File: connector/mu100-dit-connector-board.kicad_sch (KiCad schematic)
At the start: 8 parts, among them J1 Conn_01x17_Male, J2 51247 Molex, J3 JST-PH_01x10_Socket

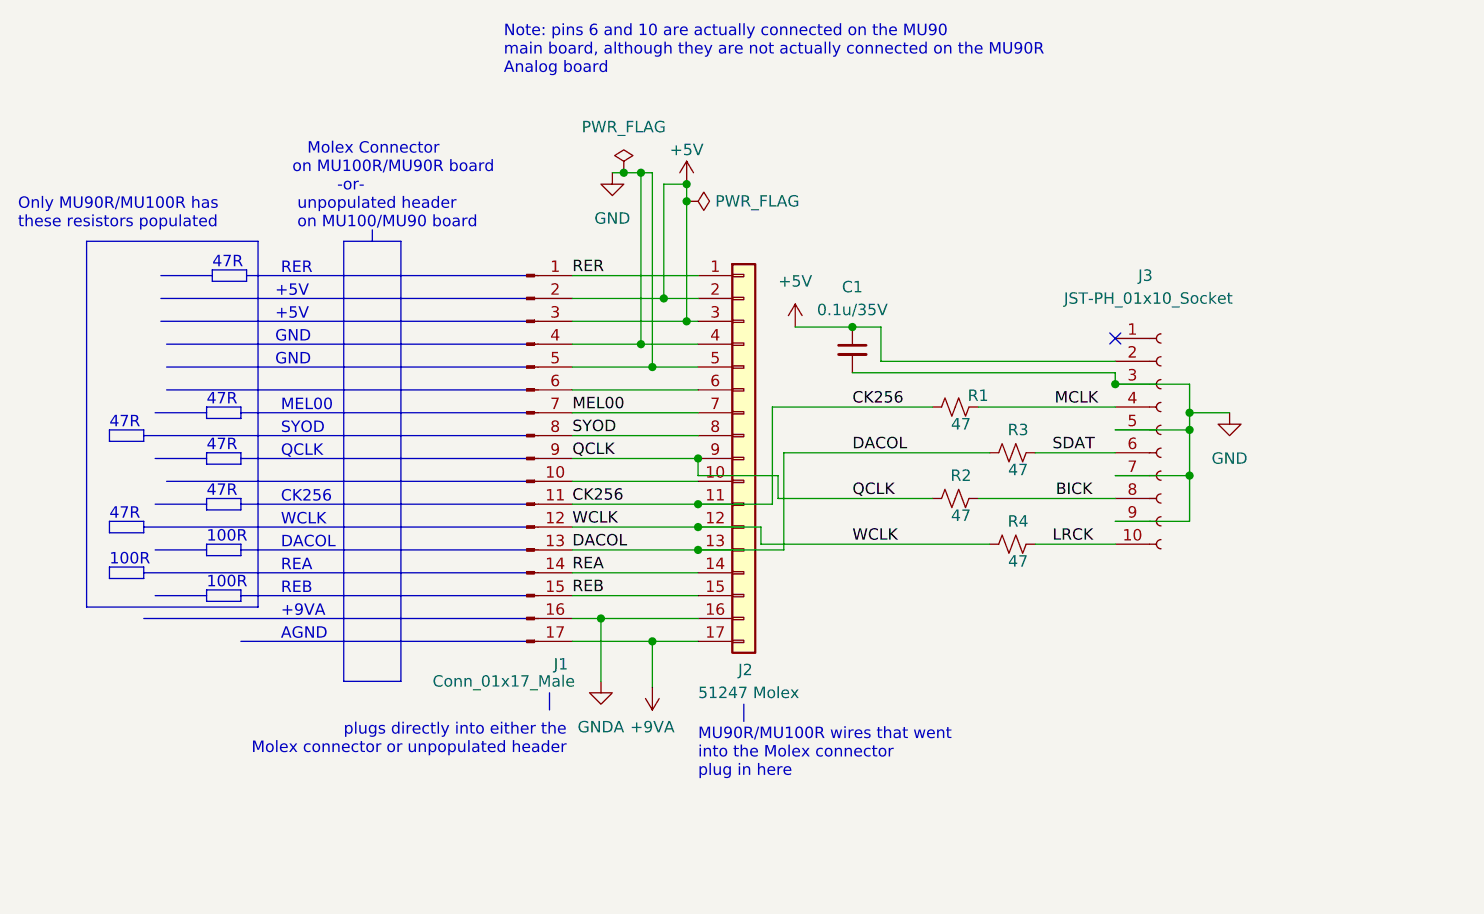
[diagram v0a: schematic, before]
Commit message: Clean up schematics and board drawings
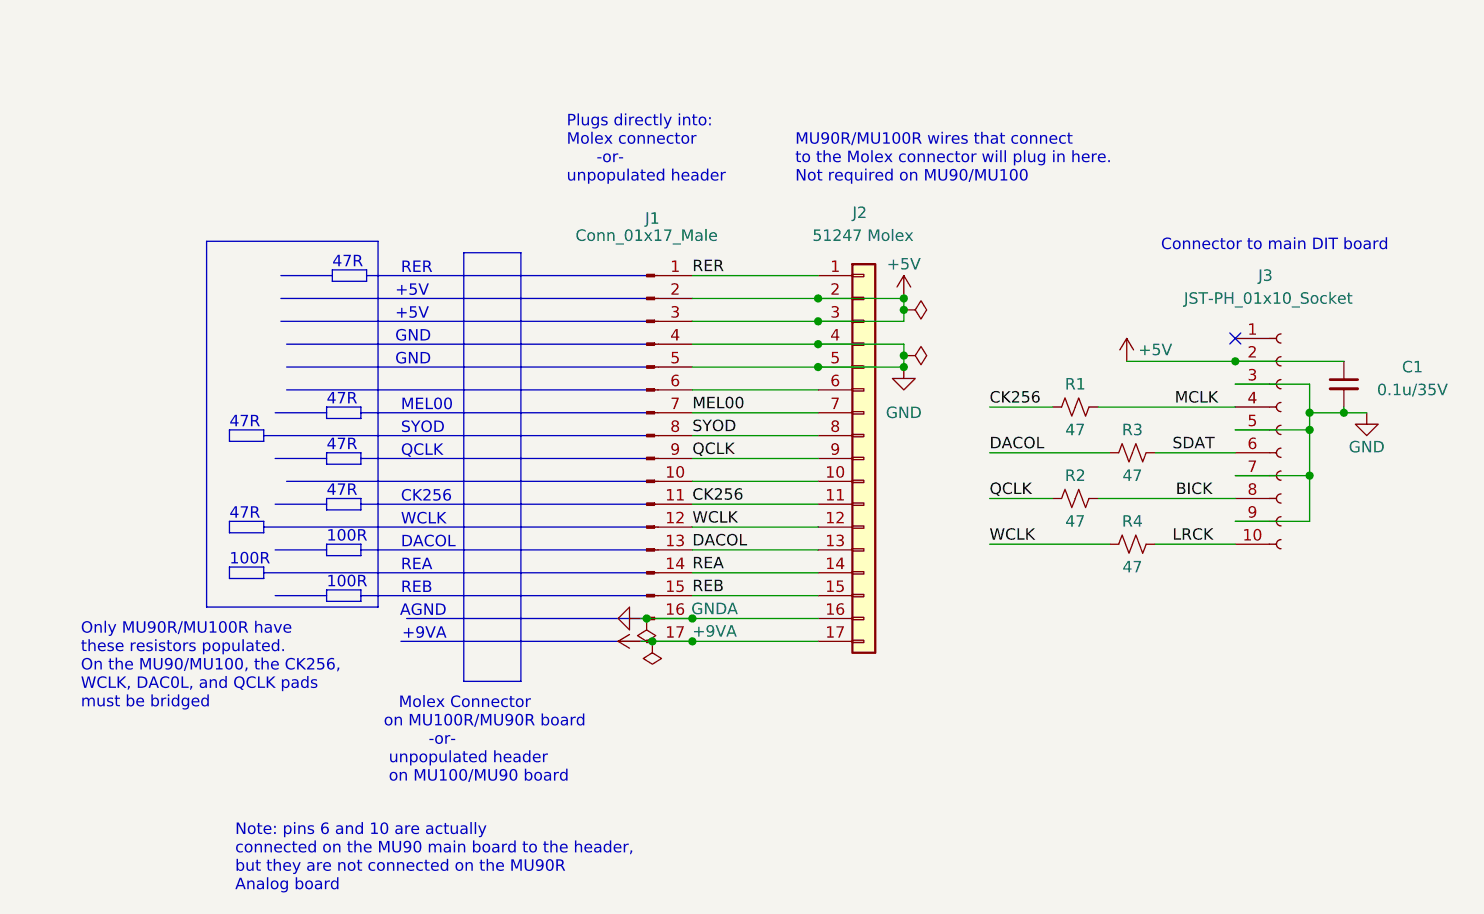
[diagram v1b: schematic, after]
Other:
- note added: "Connector to main DIT board"
- note added: "MU90R/MU100R wires that connect to the Molex connector will plug in here. Not required on MU90/MU100"
- note added: "Note: pins 6 and 10 are actually connected on the MU90 main board to the header, but they are not connected on the MU90R Analog board"
- note added: "Only MU90R/MU100R have these resistors populated. On the MU90/MU100, the CK256, WCLK, DAC0L, and QCLK pads must be bridged"
- note added: "Plugs directly into: Molex connector -or- unpopulated header"
- note removed: "MU90R/MU100R wires that went into the Molex connector plug in here"
- note removed: "Note: pins 6 and 10 are actually connected on the MU90 main board, although they are not actually connected on the MU90R Analog board"
- note removed: "Only MU90R/MU100R has these resistors populated"
- note removed: "plugs directly into either the Molex connector or unpopulated header"
- moved on the sheet: C1, J1, J2, J3, R1, R2, R3, R4

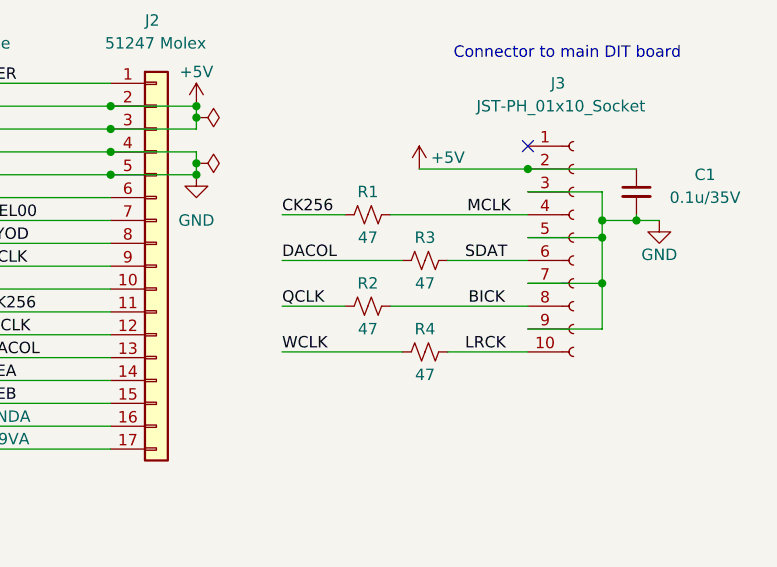
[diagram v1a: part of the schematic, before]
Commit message: remove terminating resistors on connector board
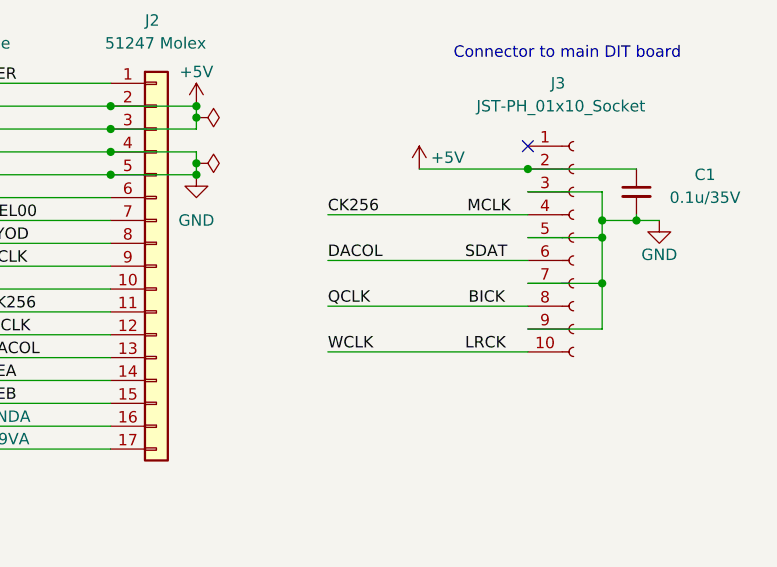
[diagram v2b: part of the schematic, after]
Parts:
- removed R1, R2, R3, R4: 47, Resistor_SMD:R_0805_2012Metric_Pad1.20x1.40mm_HandSolder, symbol Device:R_Small_US
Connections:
- net MCLK is gone; now on net CK256: J3.4 (Pin_4)
- net QCLK is gone; now on net BICK: J1.9 (Pin_9), J2.9 (Pin_9)
- net SDAT is gone; now on net DACOL: J3.6 (Pin_6)
- net WCLK is gone; now on net LRCK: J1.12 (Pin_12), J2.12 (Pin_12)
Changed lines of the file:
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@@
     (stroke (width 0) (type default) (color 0 0 0 0))
   )
-  (wire (pts (xy 121.92 88.265) (xy 128.905 88.265))
+  (wire (pts (xy 127 88.265) (xy 149.225 88.265))
     (stroke (width 0) (type default) (color 0 0 0 0))
   )
@@
     (stroke (width 0) (type default) (color 0 0 0 0))
   )
-  (wire (pts (xy 140.335 93.345) (xy 149.225 93.345))
-    (stroke (width 0) (type default) (color 0 0 0 0))
-  )
   (polyline (pts (xy 52.705 63.5) (xy 52.705 62.865))
     (stroke (width 0) (type default) (color 0 0 0 0))
@@
     (stroke (width 0) (type default) (color 0 0 0 0))
   )
-  (wire (pts (xy 121.92 93.345) (xy 135.255 93.345))
+  (wire (pts (xy 127 93.345) (xy 149.225 93.345))
     (stroke (width 0) (type default) (color 0 0 0 0))
   )
@@
     (stroke (width 0) (type default) (color 0 0 0 0))
   )
+  (wire (pts (xy 157.48 75.565) (xy 157.48 78.74))
+    (stroke (width 0) (type default) (color 0 0 0 0))
+  )
   (polyline (pts (xy 52.07 83.82) (xy 52.07 83.185))
     (stroke (width 0) (type default) (color 0 0 0 0))
@@
     (stroke (width 0) (type default) (color 0 0 0 0))
   )
-  (wire (pts (xy 133.985 88.265) (xy 149.225 88.265))
-    (stroke (width 0) (type default) (color 0 0 0 0))
-  )
   (wire (pts (xy 88.9 104.14) (xy 102.87 104.14))
     (stroke (width 0) (type default) (color 0 0 0 0))
@@
     (stroke (width 0) (type default) (color 0 0 0 0))
   )
-  (wire (pts (xy 133.985 78.105) (xy 149.225 78.105))
-    (stroke (width 0) (type default) (color 0 0 0 0))
-  )
   (polyline (pts (xy 52.07 99.695) (xy 52.07 99.06))
     (stroke (width 0) (type default) (color 0 0 0 0))
@@
     (stroke (width 0) (type default) (color 0 0 0 0))
   )
-  (wire (pts (xy 121.92 83.185) (xy 135.255 83.185))
+  (wire (pts (xy 127 83.185) (xy 149.225 83.185))
     (stroke (width 0) (type default) (color 0 0 0 0))
   )
@@
     (stroke (width 0) (type default) (color 0 0 0 0))
   )
-  (wire (pts (xy 140.335 83.185) (xy 149.225 83.185))
-    (stroke (width 0) (type default) (color 0 0 0 0))
-  )
   (wire (pts (xy 88.9 93.98) (xy 102.87 93.98))
     (stroke (width 0) (type default) (color 0 0 0 0))
@@
     (stroke (width 0) (type default) (color 0 0 0 0))
   )
-  (wire (pts (xy 121.92 78.105) (xy 128.905 78.105))
+  (wire (pts (xy 127 78.105) (xy 149.225 78.105))
     (stroke (width 0) (type default) (color 0 0 0 0))
   )
   (polyline (pts (xy 37.465 90.805) (xy 37.465 92.075))
-    (stroke (width 0) (type default) (color 0 0 0 0))
-  )
-  (wire (pts (xy 157.48 75.565) (xy 157.48 78.74))
     (stroke (width 0) (type default) (color 0 0 0 0))
   )
@@
     (effects (font (size 1.27 1.27)) (justify left bottom))
   )
-  (label "DACOL" (at 121.92 83.185 0)
+  (label "DACOL" (at 127 83.185 0)
     (effects (font (size 1.27 1.27)) (justify left bottom))
   )
@@
     (effects (font (size 1.27 1.27)) (justify left bottom))
   )
-  (label "CK256" (at 121.92 78.105 0)
+  (label "CK256" (at 127 78.105 0)
     (effects (font (size 1.27 1.27)) (justify left bottom))
   )
@@
     (effects (font (size 1.27 1.27)) (justify left bottom))
   )
-  (label "WCLK" (at 121.92 93.345 0)
+  (label "WCLK" (at 127 93.345 0)
     (effects (font (size 1.27 1.27)) (justify left bottom))
   )
@@
     (effects (font (size 1.27 1.27)) (justify left bottom))
   )
-  (label "QCLK" (at 121.92 88.265 0)
+  (label "QCLK" (at 127 88.265 0)
     (effects (font (size 1.27 1.27)) (justify left bottom))
   )
@@
     )
     (pin "1")
-  )
-  (symbol (lib_id "Device:R_Small_US") (at 137.795 93.345 90) (unit 1)
-    (in_bom yes) (on_board yes)
-    (property "Reference" "R4" (id 0) (at 137.795 90.805 90))
-    (property "Value" "47" (id 1) (at 137.795 95.885 90))
-    (property "Footprint" "Resistor_SMD:R_0805_2012Metric_Pad1.20x1.40mm_HandSolder" (id 2) (at 137.795 93.345 0)
-      (effects (font (size 1.27 1.27)) hide)
-    )
-    (property "Datasheet" "~" (id 3) (at 137.795 93.345 0)
-      (effects (font (size 1.27 1.27)) hide)
-    )
-    (pin "1")
-    (pin "2")
   )
   (symbol (lib_id "Connector:Conn_01x10_Female") (at 154.305 80.645 0) (unit 1)
@@
     (pin "9")
   )
-  (symbol (lib_id "Device:R_Small_US") (at 131.445 88.265 90) (unit 1)
-    (in_bom yes) (on_board yes)
-    (property "Reference" "R2" (id 0) (at 131.445 85.725 90))
-    (property "Value" "47" (id 1) (at 131.445 90.805 90))
-    (property "Footprint" "Resistor_SMD:R_0805_2012Metric_Pad1.20x1.40mm_HandSolder" (id 2) (at 131.445 88.265 0)
-      (effects (font (size 1.27 1.27)) hide)
-    )
-    (property "Datasheet" "~" (id 3) (at 131.445 88.265 0)
-      (effects (font (size 1.27 1.27)) hide)
-    )
-    (pin "1")
-    (pin "2")
-  )
   (symbol (lib_id "power:+5V") (at 137.16 73.025 0) (unit 1)
     (in_bom yes) (on_board yes)
@@
     )
     (pin "1")
-  )
-  (symbol (lib_id "Device:R_Small_US") (at 137.795 83.185 90) (unit 1)
-    (in_bom yes) (on_board yes)
-    (property "Reference" "R3" (id 0) (at 137.795 80.645 90))
-    (property "Value" "47" (id 1) (at 137.795 85.725 90))
-    (property "Footprint" "Resistor_SMD:R_0805_2012Metric_Pad1.20x1.40mm_HandSolder" (id 2) (at 137.795 83.185 0)
-      (effects (font (size 1.27 1.27)) hide)
-    )
-    (property "Datasheet" "~" (id 3) (at 137.795 83.185 0)
-      (effects (font (size 1.27 1.27)) hide)
-    )
-    (pin "1")
-    (pin "2")
   )
   (symbol (lib_id "Device:C_Small") (at 161.29 75.565 0) (mirror y) (unit 1)
@@
     (pin "1")
   )
-  (symbol (lib_id "Device:R_Small_US") (at 131.445 78.105 90) (unit 1)
-    (in_bom yes) (on_board yes)
-    (property "Reference" "R1" (id 0) (at 131.445 75.565 90))
-    (property "Value" "47" (id 1) (at 131.445 80.645 90))
-    (property "Footprint" "Resistor_SMD:R_0805_2012Metric_Pad1.20x1.40mm_HandSolder" (id 2) (at 131.445 78.105 0)
-      (effects (font (size 1.27 1.27)) hide)
-    )
-    (property "Datasheet" "~" (id 3) (at 131.445 78.105 0)
-      (effects (font (size 1.27 1.27)) hide)
-    )
-    (pin "1")
-    (pin "2")
-  )
   (symbol (lib_id "power:+5V") (at 112.395 66.04 0) (unit 1)
     (in_bom yes) (on_board yes)
@@
       (reference "J3") (unit 1) (value "JST-PH_01x10_Socket") (footprint "Connector_JST:JST_PH_B10B-PH-K_1x10_P2.00mm_Vertical")
     )
-    (path "/f86635c0-8741-4817-a07f-89bcb9b4e41f"
-      (reference "R1") (unit 1) (value "47") (footprint "Resistor_SMD:R_0805_2012Metric_Pad1.20x1.40mm_HandSolder")
-    )
-    (path "/62cc9f59-39d9-4772-b112-9db69118b7ea"
-      (reference "R2") (unit 1) (value "47") (footprint "Resistor_SMD:R_0805_2012Metric_Pad1.20x1.40mm_HandSolder")
-    )
-    (path "/6fa48e34-f98f-4ce1-bf74-e50b7e7d7d11"
-      (reference "R3") (unit 1) (value "47") (footprint "Resistor_SMD:R_0805_2012Metric_Pad1.20x1.40mm_HandSolder")
-    )
-    (path "/30583d87-d48d-4dd5-8dea-293a9cb913a5"
-      (reference "R4") (unit 1) (value "47") (footprint "Resistor_SMD:R_0805_2012Metric_Pad1.20x1.40mm_HandSolder")
-    )
-  )
+  )

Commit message: FInal board revision
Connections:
- net BICK renamed QCLK
- net LRCK renamed WCLK
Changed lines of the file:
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@@
     (effects (font (size 1.27 1.27)) (justify left bottom))
-  )
-  (label "LRCK" (at 142.24 93.345 0)
-    (effects (font (size 1.27 1.27)) (justify left bottom))
-  )
-  (label "MCLK" (at 147.32 78.105 180)
-    (effects (font (size 1.27 1.27)) (justify right bottom))
   )
   (label "WCLK" (at 88.9 91.44 0)
@@
     (effects (font (size 1.27 1.27)) (justify left bottom))
   )
-  (label "SDAT" (at 142.24 83.185 0)
-    (effects (font (size 1.27 1.27)) (justify left bottom))
-  )
   (label "QCLK" (at 88.9 83.82 0)
     (effects (font (size 1.27 1.27)) (justify left bottom))
@@
     (effects (font (size 1.27 1.27)) (justify left bottom))
   )
-  (label "BICK" (at 146.685 88.265 180)
-    (effects (font (size 1.27 1.27)) (justify right bottom))
-  )
   (label "SYOD" (at 88.9 81.28 0)
